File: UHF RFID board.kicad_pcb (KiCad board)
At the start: 2 copper layers, 67.3 x 36.7 mm, 30 parts, among them J1 FZ_full_module, J10 SIM_Card, J11 SIM_Card, J2 picoblade, J3 Conn_02x04_Odd_Even, J4 Conn_02x03_Odd_Even, U1 YRM1001, U2 SEC1210

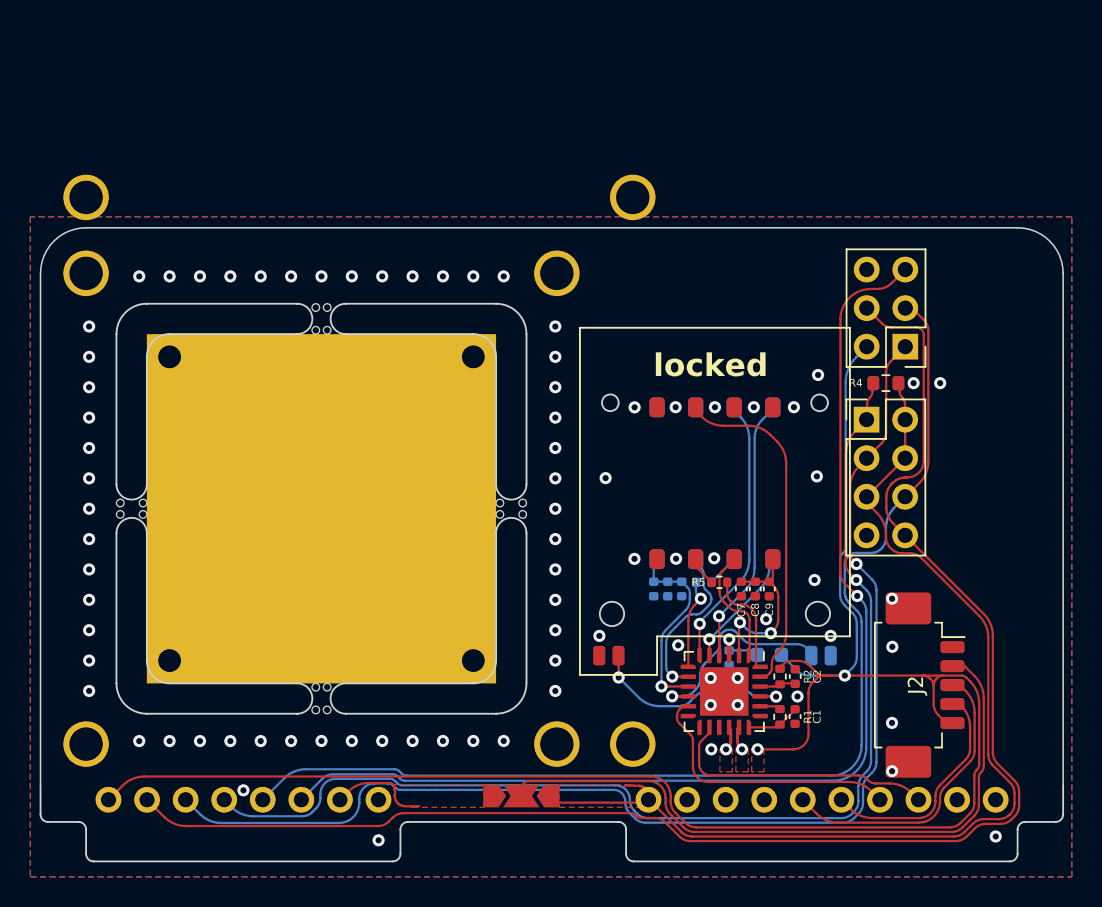
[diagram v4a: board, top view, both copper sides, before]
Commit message: Update V2.1
- modified schematic to add iClass SE processor chip connections and symbol
- added footprints to enable direct mounting of iClass SE processor chips instead of using a SAM (https://www.hidglobal.com/products/sio-processor)
- added e.e.
- routing
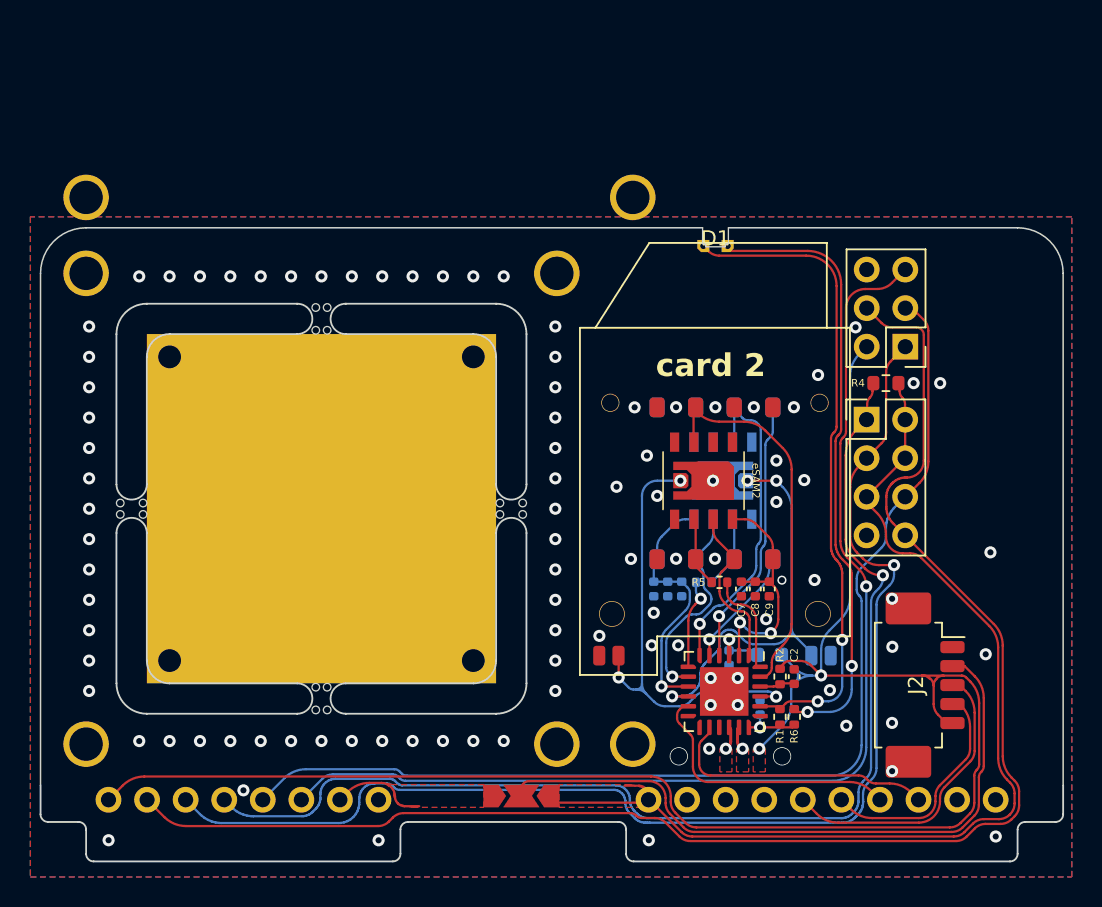
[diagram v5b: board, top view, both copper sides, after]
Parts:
- added D1: LED, Custom LEDs:side-edge mount, F.Cu at (162.8, 95.6)
- added R6: 330R, Resistor_SMD:R_0402_1005Metric, F.Cu at (168.0, 127.8)
- added eSAM1: ~, Custom footprints:DFN-8-1EP_5x5mm_P1.27mm_EP2.5x4mm, B.Cu at (163.3, 112.2)
- added eSAM2: ~, Custom footprints:DFN-8-1EP_5x5mm_P1.27mm_EP2.5x4mm, F.Cu at (162.0, 112.2)
- C1: moved to B.Cu
- J3: value Conn_02x04_Odd_Even -> SPI
- J4: value Conn_02x03_Odd_Even -> ICSP
- moved C1 2.39 mm to (165.8, 127.2), turned to 90 degrees
- moved REF** 0.28 mm to (163.8, 130.7)
- moved C2 0.07 mm to (168.0, 125.2)
- renumbered J10 to SAM1, J11 to SAM2
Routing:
- net /LED_ACT: track 1.30 -> 42.8 mm, vias 0 -> 2
- net Net-(D1-A): track 0.00 -> 40.7 mm, vias 0 -> 2
- net /SC2_PRsNT: track 14.0 -> 31.1 mm, vias 2 -> 3
- net /SC1_PRSNT: track 13.7 -> 27.9 mm, vias 1 -> 3
- net /SC2_VCC: track 11.6 -> 16.0 mm
- net /SC1_VCC: track 12.9 -> 17.0 mm
- net /SC1_IO: track 18.0 -> 21.7 mm
- net /SC2_RST: track 7.86 -> 11.0 mm
- net /SC1_RST: track 10.9 -> 14.0 mm
- net +5V: track 123.2 -> 120.2 mm
- net /SC2_CLK: track 1.96 -> 4.65 mm
- net /SC2_IO: track 22.8 -> 25.3 mm
- net /SC1_CLK: track 2.05 -> 4.42 mm
- net MISO: track 80.9 -> 82.9 mm
- net CLK: track 74.3 -> 72.7 mm
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- added copper zone on B.Cu, net +5V
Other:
- outline, holes or cut-outs redrawn
- board text added: "Sam? Who's Sam?"
- board text added: "UHF | RFID | SAM Version 2.1"
- board text added: "card 1"
- board text added: "card 2"
- board text added: "https://github.com/Didgitalpunk/"
- board text removed: "UHF | RFID | SAM Version 2.O"
- board text removed: "locked"

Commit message: fixes + bom, end of work on V2
Fixed some footprint directory inconsistencies and errors dating form at least the start of the SAM integration phase for some, Cleaned up / reworked some footprints and finalized others.
Fixed some BOM links being incorrect and/or missing.

That concludes work on V2. Next additions will go towards V3 if there ever is one, but the board is now getting very cramped, and will be in a branch now that I know how those work.
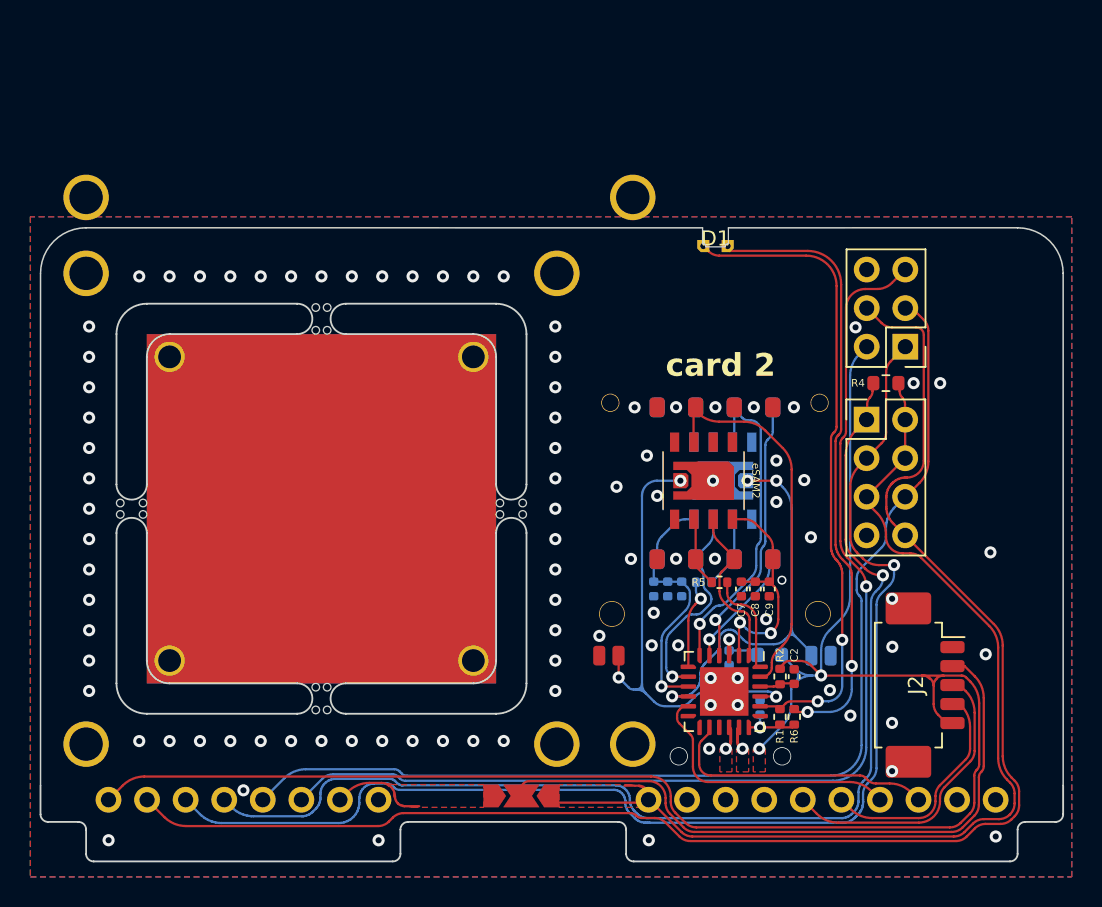
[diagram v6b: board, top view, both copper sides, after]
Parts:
- removed GuhfRfid: LOGO, LOGO
- removed REF**: kapton tape 5x3, custom misc:kapton tape 5x3
- added [UHF | RFID for Flipper] repo by Frux: [UHF RFID for Flipper] repo by Frux, Logos:[UHF RFID for Flipper] repo by Frux, F.Cu at (136.9, 114.1)
- G***: value LOGO -> Flippermeister; footprint LOGO -> Logos:Flippermeister
- SAM1, SAM2: footprint Custom footprints:SIMMP-00801B000-G sim card connector -> Custom footprints:SIMMP-00801B000-G sim card connector w plated holes
- [Seader] repo by Bettse: renamed from Gnard; value LOGO -> [Seader] repo by Bettse; footprint LOGO -> Logos:[Seader] repo by Bettse
- eSAM1, eSAM2: footprint Custom footprints:DFN-8-1EP_5x5mm_P1.27mm_EP2.5x4mm -> Custom footprints:DFN-8-splitEP_5x5mm_P1.27mm_EP2.5x4mm
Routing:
- net GND: vias 98 -> 97
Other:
- board text added: "UHF RFID"
- board text added: "UHF | RFID | SAM Version 2.2"
- board text removed: "UHF | RFID | SAM Version 2.1"
- board text removed: "[Seader] repo by Bettse"
- board text removed: "[UHF | RFID for Flipper] repo by Frux"

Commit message: V2.3 release
Switched a resistor and capacitor to B.cu to ensure they don't get ripped off when removing the picoblade connector. depending on further testing to see if I can get the LEDout working on the SEC chip, might do the same with R1 and remove D1 and D2 and the associated resistor. 
Cleaned up routing a bit due to that change.
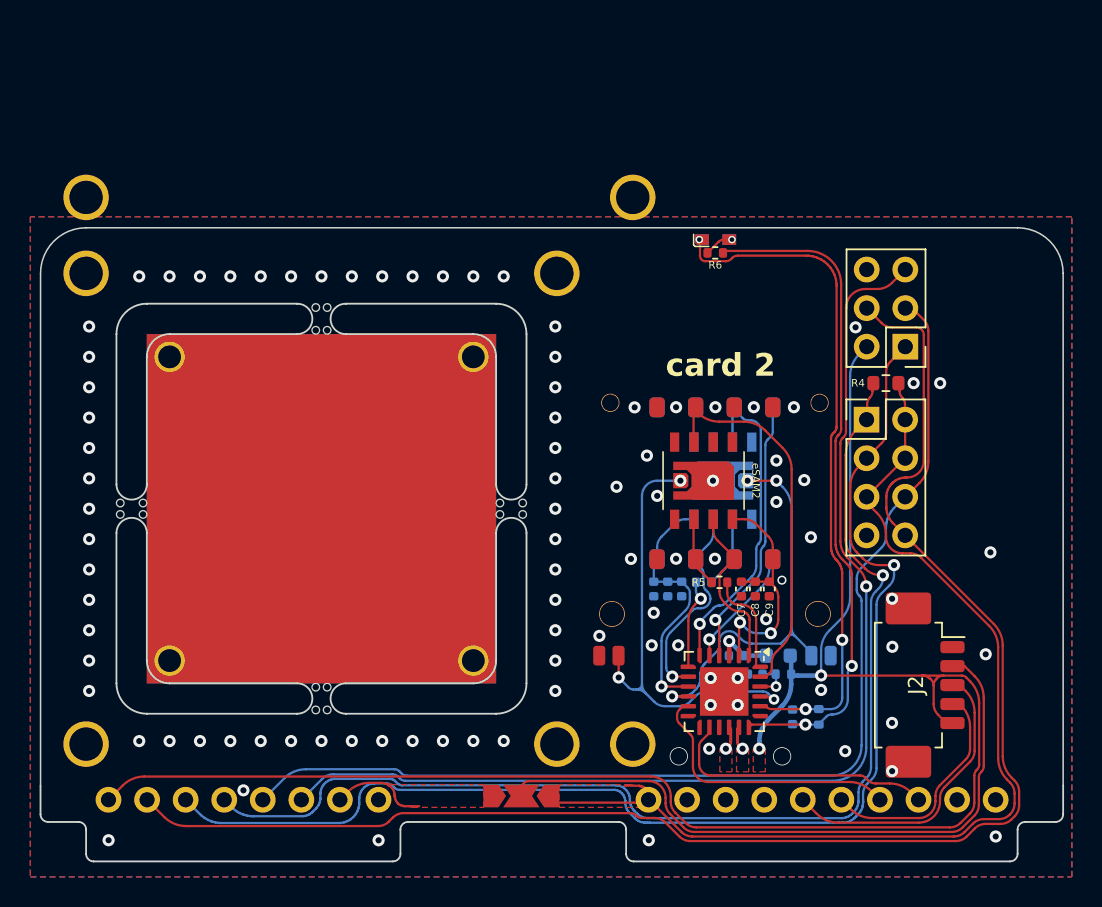
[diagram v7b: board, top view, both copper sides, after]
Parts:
- added D2: LED, Custom LEDs:kingbright AGPA1602 - FLIPPED, B.Cu at (162.8, 96.4)
- C2, R1, R2: moved to B.Cu
- D1: footprint Custom LEDs:side-edge mount -> Custom LEDs:kingbright AGPA1602
- R6: value 330R -> 33R
- moved R6 31.0 mm to (162.8, 97.2), turned to 0 degrees
- moved C2 2.57 mm to (165.4, 125.0), turned to 180 degrees
- moved R1 2.56 mm to (169.6, 127.8)
- moved C1 2.23 mm to (167.9, 127.8)
- moved D1 0.78 mm to (162.8, 96.4)
- moved L1 0.58 mm to (166.9, 123.8)
- moved C3 0.49 mm to (164.2, 123.8), turned to 180 degrees
- moved R2 0.27 mm to (167.3, 125.0), turned to 180 degrees
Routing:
- net +3.3VA: track 3.96 -> 45.1 mm, vias 1 -> 2
- net Net-(D1-A): track 40.7 -> 1.77 mm, vias 2 -> 1
- net +5V: track 120.2 -> 115.1 mm
- net /LED_ACT: track 42.8 -> 45.0 mm, vias 2 -> 3
- net /~{RESET}: track 2.26 -> 2.58 mm, vias 0 -> 1
- removed copper zone on B.Cu, net +5V
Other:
- outline, holes or cut-outs redrawn
- board text added: "UHF | RFID | SAM Version 2.3"
- board text removed: "UHF | RFID | SAM Version 2.2"

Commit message: fixed some rounded tracks that were no longer arcs
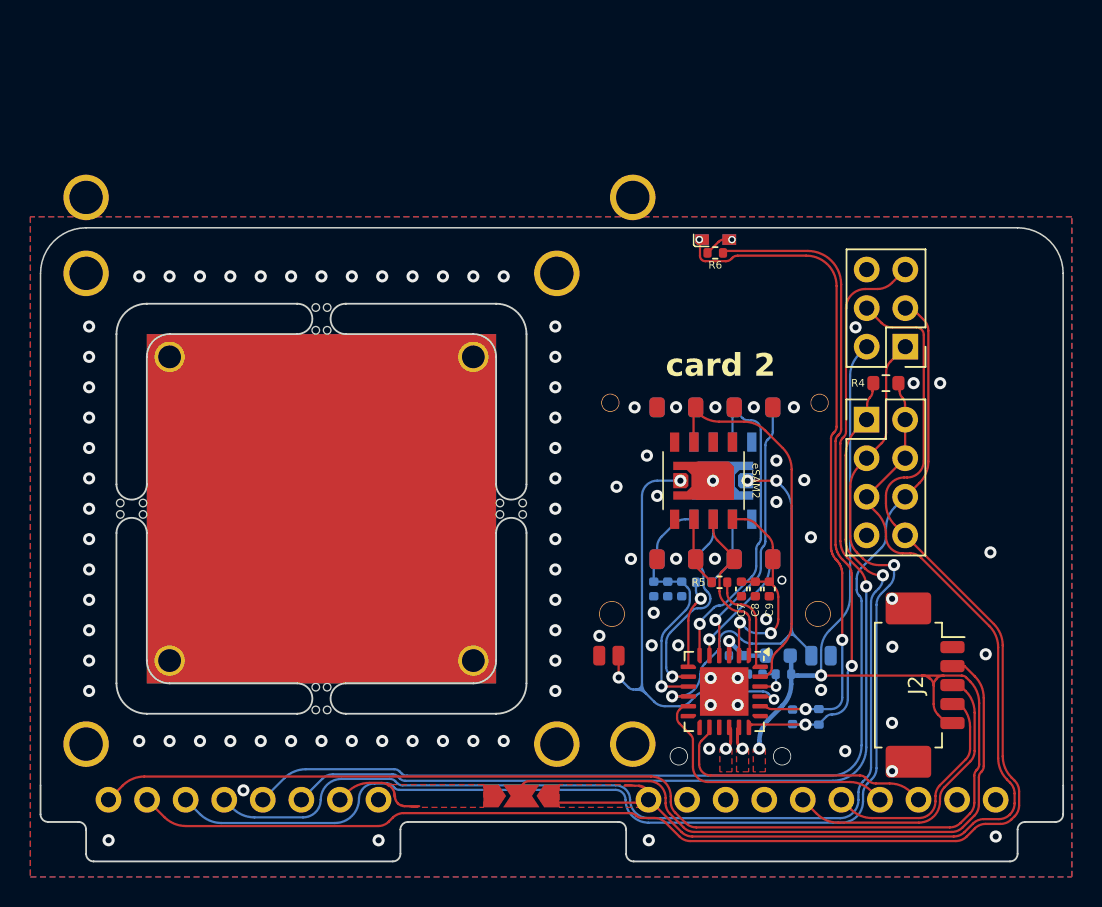
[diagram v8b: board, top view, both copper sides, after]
